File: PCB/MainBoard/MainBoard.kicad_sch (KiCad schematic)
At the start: 12 parts, among them J1 Conn_01x04_12864, J2 Conn_01x03_Female, J3 Conn_01x03_Female, SW1 RotaryEncoder_Switch, U2 Pico

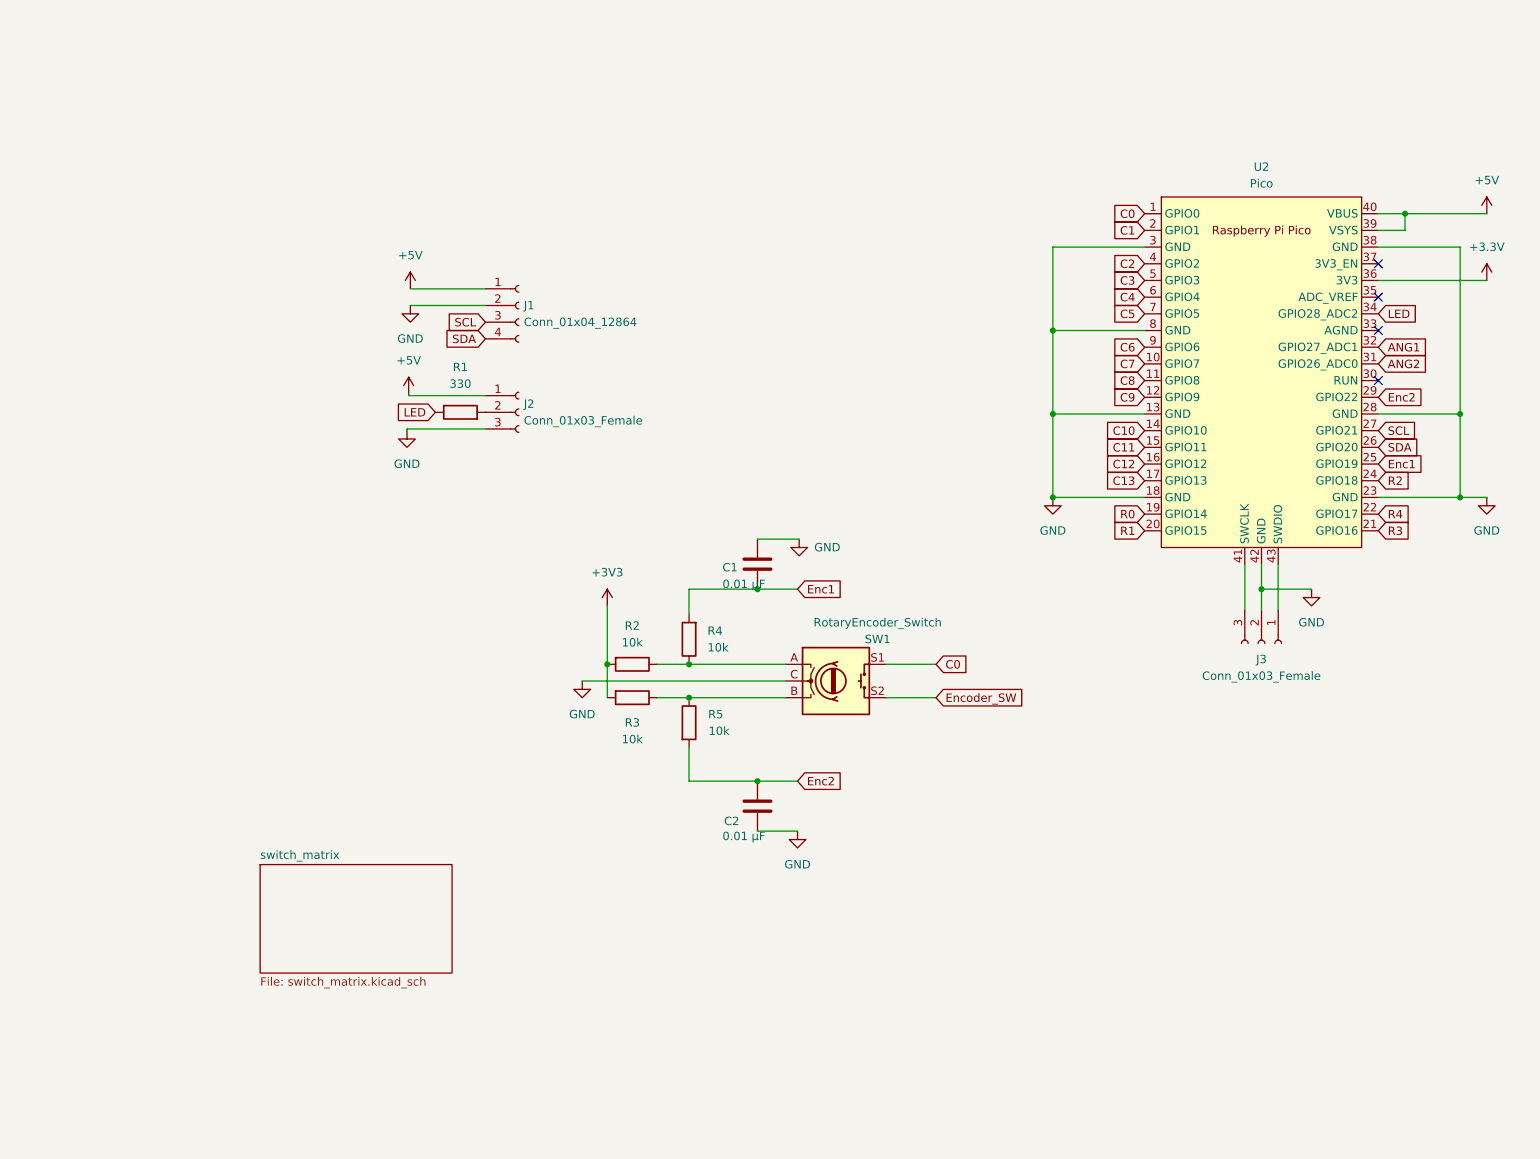
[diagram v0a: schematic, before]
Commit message: Added diodes for the duplex layout
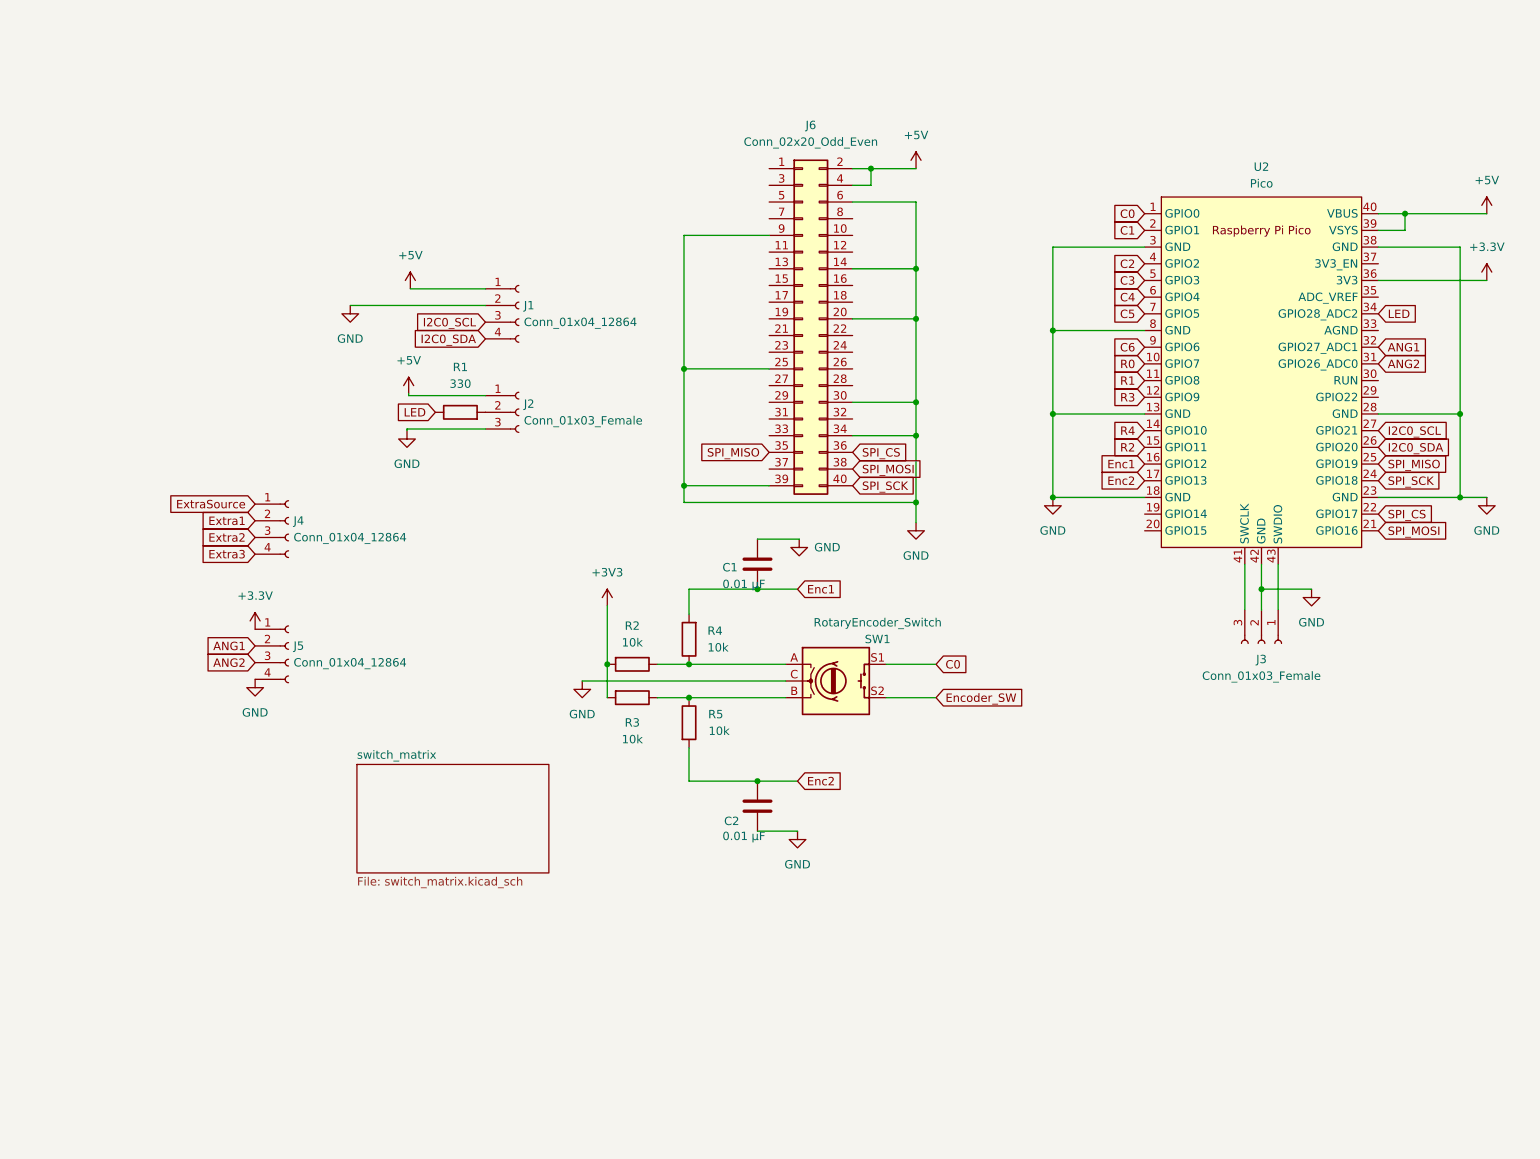
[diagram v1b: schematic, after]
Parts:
- added J4, J5: Conn_01x04_12864, Connector_JST:JST_PH_S4B-PH-K_1x04_P2.00mm_Horizontal, symbol Connector:Conn_01x04_Female
- added J6: Conn_02x20_Odd_Even, PiZero:Raspberry_Pi_Zero_Socketed_THT_MountingHoles_Castellated, symbol Connector_Generic:Conn_02x20_Odd_Even
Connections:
- net C10 is gone; now on net R4: U2.14 (GPIO10)
- net C11 is gone; now on net R2: U2.15 (GPIO11)
- net C12 is gone; now on net Enc1: U2.16 (GPIO12)
- net C13 is gone; now on net Enc2: U2.17 (GPIO13)
- net C7 is gone; now on net R0: U2.10 (GPIO7)
- net C8 is gone; now on net R1: U2.11 (GPIO8)
- net C9 is gone; now on net R3: U2.12 (GPIO9)
- net +3V3: now also J5.1 (Pin_1)
- net +5V: now also J6.2 (Pin_2), J6.4 (Pin_4)
- net ANG1: now also J5.2 (Pin_2)
- net ANG2: now also J5.3 (Pin_3)
- net Enc1: no longer U2.25 (GPIO19)
- net Enc2: no longer U2.29 (GPIO22)
- net GND: now also J5.4 (Pin_4), J6.14 (Pin_14), J6.20 (Pin_20), J6.25 (Pin_25), J6.30 (Pin_30), J6.34 (Pin_34), J6.39 (Pin_39), J6.6 (Pin_6), J6.9 (Pin_9)
- net R0: no longer U2.19 (GPIO14)
- net R1: no longer U2.20 (GPIO15)
- net R2: no longer U2.24 (GPIO18)
- net R3: no longer U2.21 (GPIO16)
- net R4: no longer U2.22 (GPIO17)
- net SCL renamed I2C0_SCL
- net SDA renamed I2C0_SDA
- new net Extra1: J4.2 (Pin_2)
- new net Extra2: J4.3 (Pin_3)
- new net Extra3: J4.4 (Pin_4)
- new net ExtraSource: J4.1 (Pin_1)
- new net SPI_CS: J6.36 (Pin_36), U2.22 (GPIO17)
- new net SPI_MISO: J6.35 (Pin_35), U2.25 (GPIO19)
- new net SPI_MOSI: J6.38 (Pin_38), U2.21 (GPIO16)
- new net SPI_SCK: J6.40 (Pin_40), U2.24 (GPIO18)
- no-connect marks 4 -> 0

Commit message: Updated 3d model
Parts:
- renumbered J6 to J2, J2 to J3, J3 to J5, J5 to J6, R4 to R2, R2 to R3, R3 to R4, U2 to U1
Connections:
- net C0: no longer SW1.S1
- net Encoder_SW renamed Encoder_SW_1
- new net Encoder_SW_2: SW1.S1
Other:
- moved on the sheet: J1, J3, J4, J6, R1

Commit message: Layout settled
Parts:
- removed J5: Conn_01x03_Female, Connector_PinHeader_2.54mm:PinHeader_1x03_P2.54mm_Vertical, symbol Connector:Conn_01x03_Female
- added J1: PiPowerSwitch, Connector_PinHeader_2.54mm:PinHeader_1x03_P2.54mm_Vertical, symbol Connector:Conn_01x03_Female
- added J3: I2C0, Connector_PinHeader_2.54mm:PinHeader_1x04_P2.54mm_Horizontal, symbol Connector:Conn_01x04_Female
- added SW1: SPI_SW, Button_Switch_THT:SW_DIP_SPSTx04_Slide_6.7x11.72mm_W7.62mm_P2.54mm_LowProfile, symbol Switch:SW_DIP_x04
- J2: value Conn_02x20_Odd_Even -> Pi_Zero
- J4: renamed from J1; value Conn_01x04_12864 -> JMD0.96C
- J5: renamed from J3; value Conn_01x03_Female -> WS2812; footprint Connector_PinHeader_2.54mm:PinHeader_1x03_P2.54mm_Vertical -> Connector_PinHeader_2.54mm:PinHeader_1x03_P2.54mm_Horizontal
- J6: renamed from J4; value Conn_01x04_12864 -> Extra_Keys
- J8: renamed from J6; value Conn_01x04_12864 -> JoyStick_Or_I2C1
- renumbered SW1 to SW2
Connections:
- net +3V3: now also J3.3 (Pin_3)
- net +5V: now also J1.1 (Pin_1), J1.2 (Pin_2); no longer J2.2 (Pin_2), J2.4 (Pin_4), U1.39 (VSYS)
- net GND: now also J3.4 (Pin_4); no longer U1.42 (GND)
- net I2C0_SCL: now also J3.1 (Pin_1)
- net I2C0_SDA: now also J3.2 (Pin_2)
- net SPI_CS: now also SW1.8; no longer J2.36 (Pin_36)
- net SPI_MISO: now also SW1.5; no longer J2.35 (Pin_35)
- net SPI_MOSI: now also SW1.7; no longer J2.38 (Pin_38)
- net SPI_SCK: now also SW1.6; no longer J2.40 (Pin_40)
- new net PI_SPI_CS: J2.36 (Pin_36), SW1.1
- new net PI_SPI_MISO: J2.35 (Pin_35), SW1.4
- new net PI_SPI_MOSI: J2.38 (Pin_38), SW1.2
- new net PI_SPI_SCK: J2.40 (Pin_40), SW1.3
- new net Pi_VCC: J1.3 (Pin_3), J2.2 (Pin_2), J2.4 (Pin_4)
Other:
- moved on the sheet: C1, C2, J2, J4, J5, J6, J8, R1, R2, R3, R4, R5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

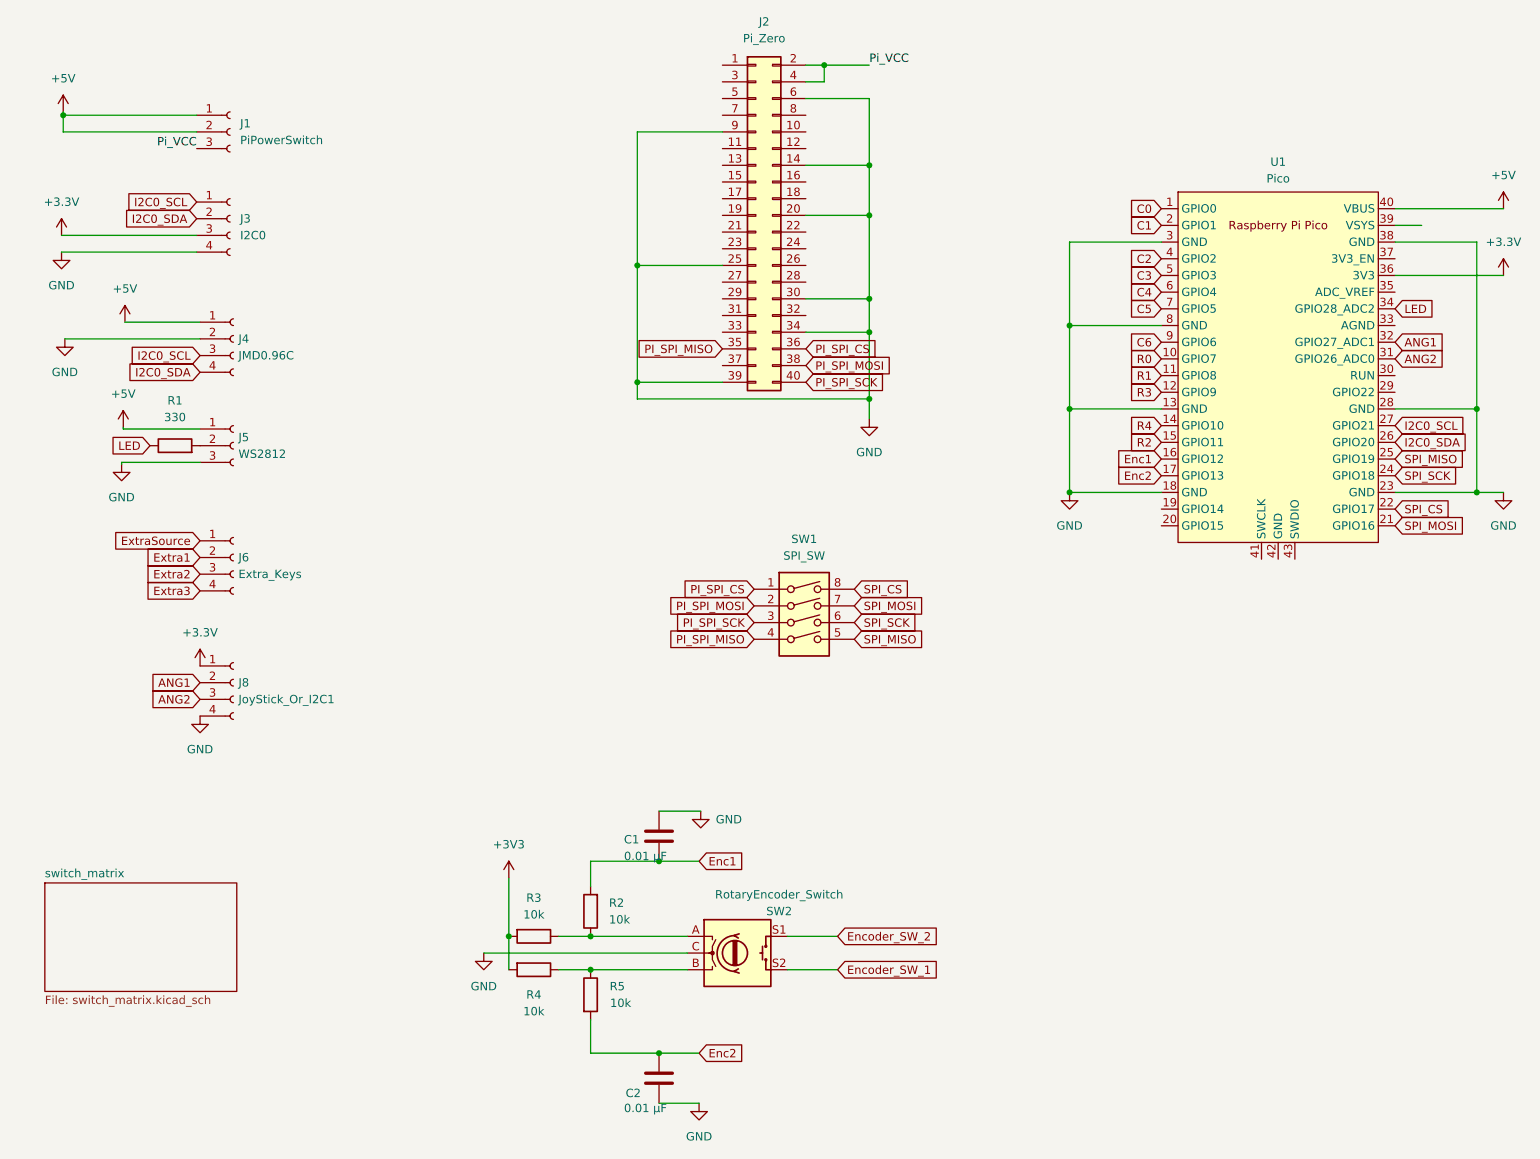
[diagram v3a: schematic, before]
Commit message: Updated layout to add mounting holes
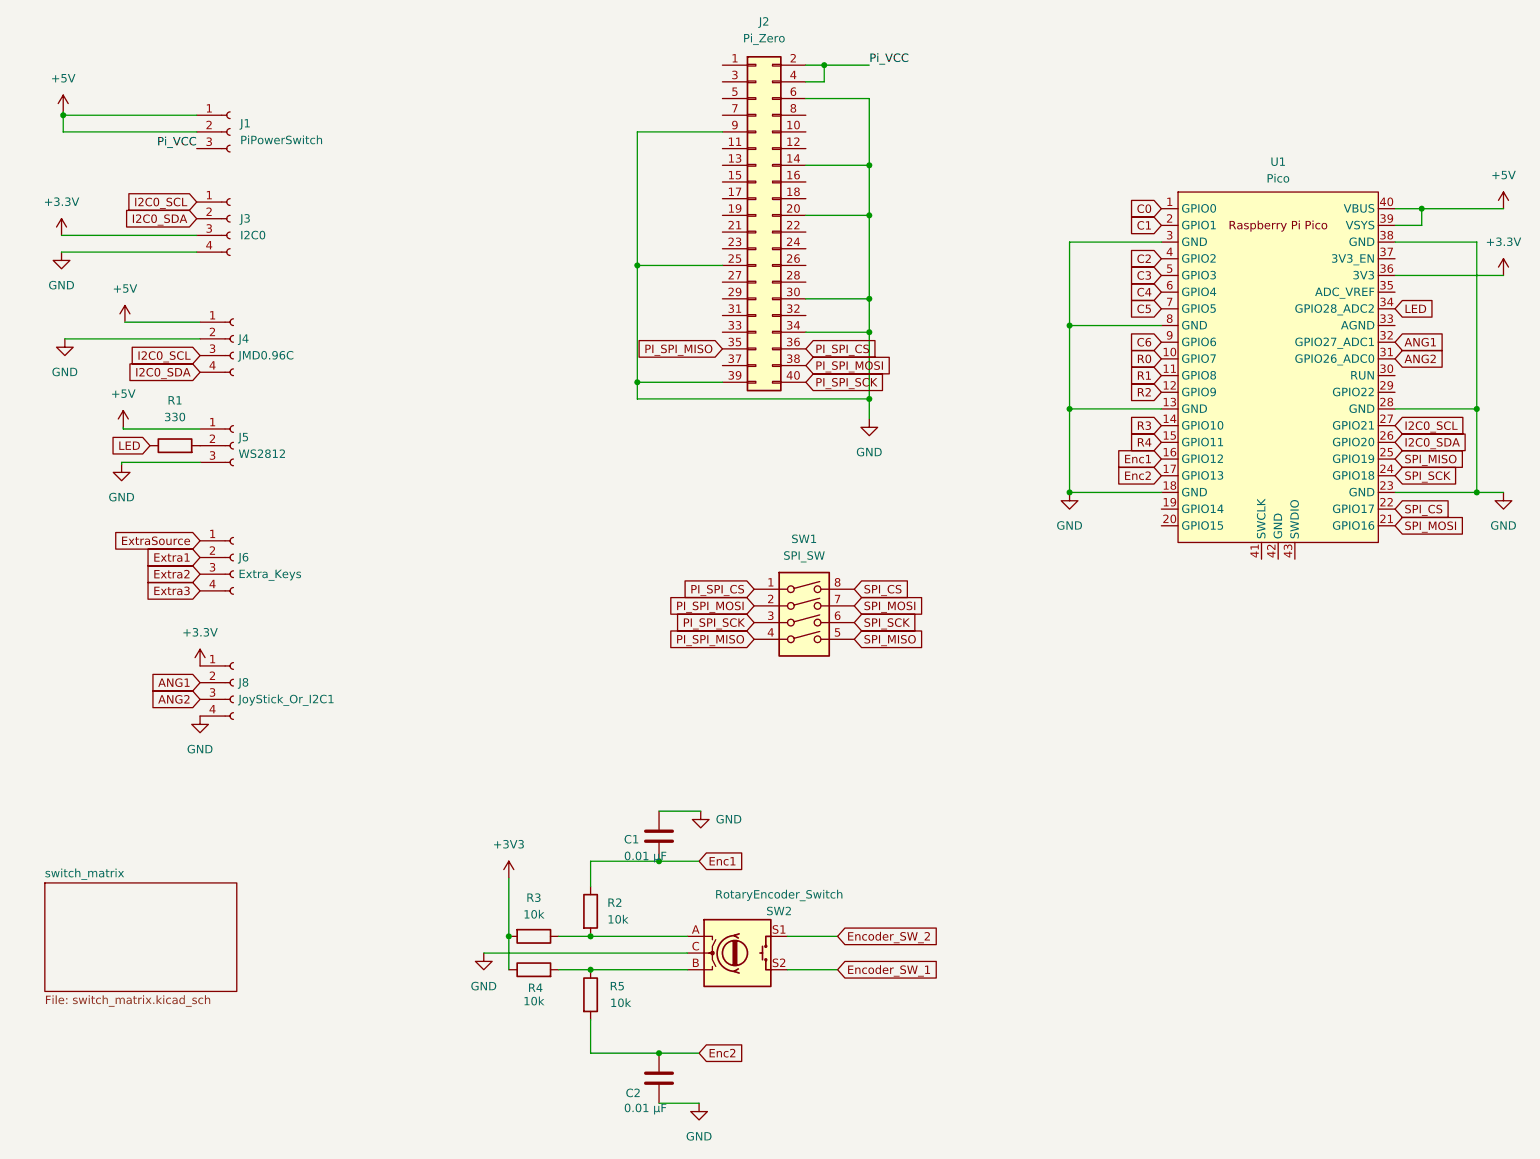
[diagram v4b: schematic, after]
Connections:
- net +3V3: now also R4.1; no longer R4.2
- net +5V: now also U1.39 (VSYS)
- net Enc1: now also R2.1; no longer R2.2
- net R2: now also U1.12 (GPIO9); no longer U1.15 (GPIO11)
- net R3: now also U1.14 (GPIO10); no longer U1.12 (GPIO9)
- net R4: now also U1.15 (GPIO11); no longer U1.14 (GPIO10)
- net at R5.1, SW2.B: now also R4.2; no longer R4.1
- net at R3.1, SW2.A: now also R2.2; no longer R2.1
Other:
- moved on the sheet: R2, R4

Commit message: Whatever
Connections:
- net C0: now also U1.9 (GPIO6); no longer U1.1 (GPIO0)
- net C1: now also U1.7 (GPIO5); no longer U1.2 (GPIO1)
- net C2: now also U1.6 (GPIO4); no longer U1.4 (GPIO2)
- net C4: now also U1.4 (GPIO2); no longer U1.6 (GPIO4)
- net C5: now also U1.2 (GPIO1); no longer U1.7 (GPIO5)
- net C6: now also U1.1 (GPIO0); no longer U1.9 (GPIO6)
